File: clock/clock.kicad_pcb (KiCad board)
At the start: 2 copper layers, 176.8 x 81.3 mm, 345 parts, among them P101 CONN_01X03, P102 CONN_FAN_PWM, P103 XG4A-1631, P301 MCRF, P401 CONN_01X10, Q201 MMBT3904, Q301 BSS138, Q302 BSS138, Q401 BSS138, Q402 BSS138, Q501 BSS138, Q502 BSS138, U201 PCA9306, U202 DAC8830, U203 LMV722, U204 LTC2990, U205 LP3853, U207 NC7SZ125, U301 Adafruit746, U302 MIC5225, U303 PA6H, U401 74LVC541, U501 TPS56428, U502 TPS56428, U503 TPS56428, U601 ADT7410, U602 DS3231, U603 ADT7410, Y202 CX210

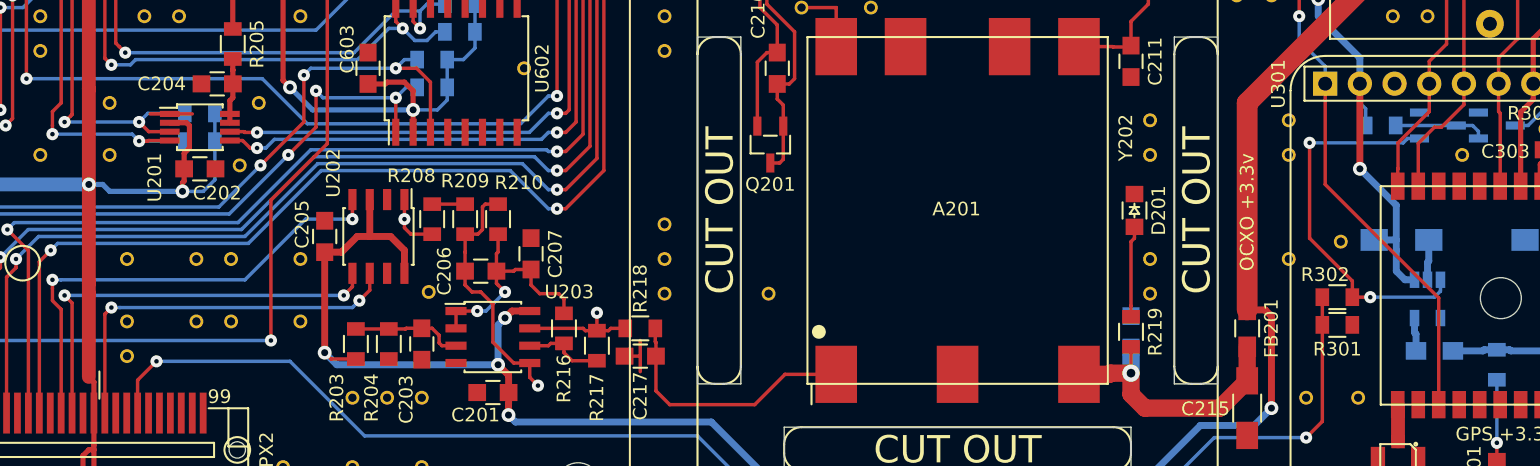
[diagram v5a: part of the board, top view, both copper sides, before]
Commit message: Add DNP to unused resistors on the termination board. Minor clean up of clock board.
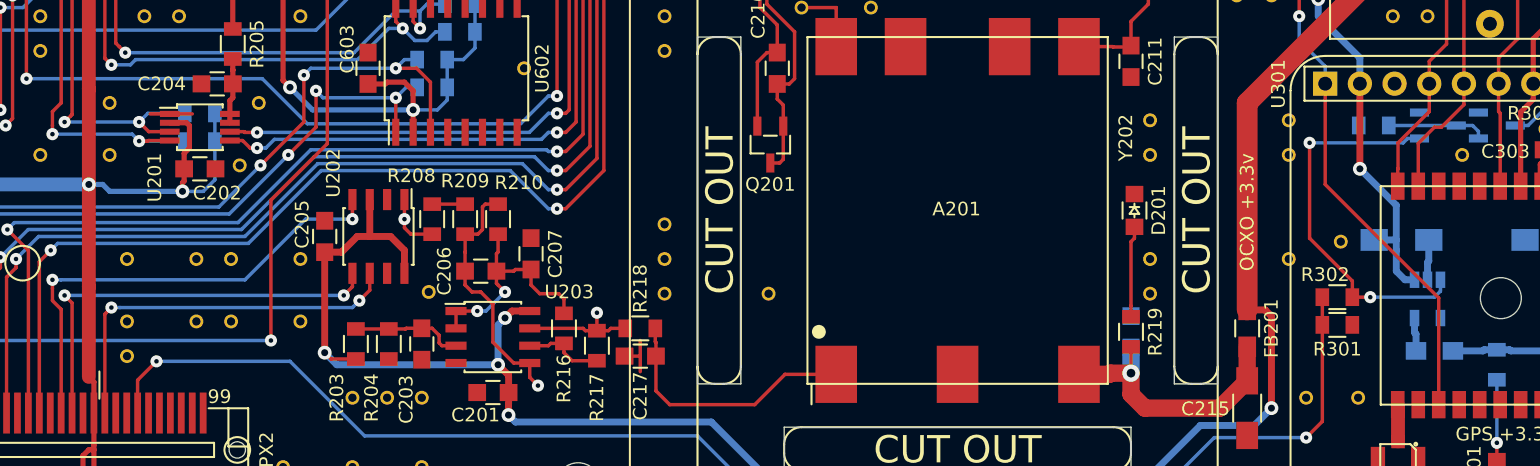
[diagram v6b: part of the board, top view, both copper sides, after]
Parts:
- moved R304 0.51 mm to (346.6, 216.3)
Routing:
- net /gps/~ENA5~: track 6.76 -> 7.27 mm
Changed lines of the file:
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@@
   (general
     (links 646)
-    (no_connects 1)
+    (no_connects 0)
     (area 184.650999 163.286 373.199858 248.171)
     (thickness 1.6)
     (drawings 90)
-    (tracks 1811)
+    (tracks 1809)
     (zones 0)
     (modules 345)
@@
   )
   (module local:R_0805_HandSoldering (layer B.Cu)
-    (at 347.091 216.281 180)
+    (at 346.583 216.281 180)
     (descr "Resistor SMD 0805, hand soldering")
     (tags "resistor 0805")
@@
   (via (at 254 184.404) (size 1.016) (drill 0.6096) (layers F.Cu B.Cu) (net 2))
   (segment (start 233.901 215.646) (end 236.728 215.646) (width 0.381) (layer F.Cu) (net 2) (status 10))
+  (segment (start 252.476 234.696) (end 252.476 228.092) (width 1.016) (layer F.Cu) (net 3))
+  (segment (start 252.476 228.092) (end 252.476 220.598978) (width 1.016) (layer F.Cu) (net 3))
   (segment (start 364.617 197.655) (end 363.771 197.655) (width 0.254) (layer F.Cu) (net 3))
   (segment (start 363.771 197.655) (end 363.601 197.485) (width 0.254) (layer F.Cu) (net 3))
@@
   (via (at 276.225 215.138) (size 1.016) (drill 0.508) (layers F.Cu B.Cu) (net 3))
   (segment (start 361.569 197.485) (end 362.491 197.485) (width 0.381) (layer F.Cu) (net 3) (status 20))
-  (segment (start 252.476 234.696) (end 252.476 228.6) (width 1.016) (layer F.Cu) (net 3))
-  (segment (start 252.476 228.6) (end 252.476 227.838) (width 1.016) (layer F.Cu) (net 3))
-  (segment (start 252.476 227.838) (end 252.476 220.598978) (width 1.016) (layer F.Cu) (net 3))
   (via (at 252.476 220.598978) (size 1.016) (drill 0.508) (layers F.Cu B.Cu) (net 3))
   (segment (start 252.476 213.614008) (end 252.476 220.598978) (width 1.016) (layer F.Cu) (net 3))
   (segment (start 252.476006 213.614002) (end 252.476 213.614008) (width 1.016) (layer F.Cu) (net 3))
+  (segment (start 345.483 216.281) (end 345.483 214.968) (width 0.254) (layer B.Cu) (net 4))
+  (segment (start 345.483 214.968) (end 345.567 214.884) (width 0.254) (layer B.Cu) (net 4))
+  (segment (start 345.567 214.884) (end 345.567 213.217) (width 0.254) (layer B.Cu) (net 4))
   (segment (start 348.234 225.425) (end 348.234 224.663) (width 0.508) (layer B.Cu) (net 4))
   (segment (start 348.234 224.663) (end 348.234 222.123) (width 0.508) (layer B.Cu) (net 4))
@@
   (segment (start 345.567 219.456006) (end 345.567 213.217) (width 0.508) (layer F.Cu) (net 4))
   (segment (start 345.567 211.328) (end 345.567 213.217) (width 0.508) (layer B.Cu) (net 4))
-  (segment (start 345.567 213.217) (end 345.567 214.63) (width 0.254) (layer B.Cu) (net 4))
-  (segment (start 345.991 215.054) (end 345.567 214.63) (width 0.254) (layer B.Cu) (net 4))
-  (segment (start 345.991 216.281) (end 345.991 215.054) (width 0.254) (layer B.Cu) (net 4))
   (via (at 345.567 219.456006) (size 1.016) (drill 0.508) (layers F.Cu B.Cu) (net 4))
   (segment (start 318.008 178.181) (end 319.906 178.181) (width 0.508) (layer B.Cu) (net 5))
@@
   (segment (start 271.145 228.727) (end 271.78 228.092) (width 0.254) (layer F.Cu) (net 49))
   (segment (start 271.78 228.092) (end 271.78 227.109) (width 0.254) (layer F.Cu) (net 49))
-  (segment (start 271.78 229.616) (end 254.755617 229.616) (width 0.254) (layer B.Cu) (net 50))
-  (segment (start 272.288 229.108) (end 271.78 229.616) (width 0.254) (layer B.Cu) (net 50))
-  (segment (start 253.682501 230.060499) (end 254.127 229.616) (width 0.254) (layer F.Cu) (net 50))
   (segment (start 253.6472 237.3427) (end 253.6472 230.0958) (width 0.254) (layer F.Cu) (net 50))
-  (segment (start 253.6472 230.0958) (end 253.682501 230.060499) (width 0.254) (layer F.Cu) (net 50))
+  (segment (start 253.6472 230.0958) (end 253.746 229.997) (width 0.254) (layer F.Cu) (net 50))
+  (segment (start 253.746 229.997) (end 254.127 229.616) (width 0.254) (layer F.Cu) (net 50))
   (segment (start 254.755617 229.616) (end 254.127 229.616) (width 0.254) (layer B.Cu) (net 50))
+  (segment (start 271.78 229.616) (end 254.755617 229.616) (width 0.254) (layer B.Cu) (net 50))
+  (segment (start 272.288 229.108) (end 271.78 229.616) (width 0.254) (layer B.Cu) (net 50))
   (via (at 254.127 229.616) (size 0.889) (drill 0.3302) (layers F.Cu B.Cu) (net 50))
-  (segment (start 254.508 229.616) (end 254.127 229.616) (width 0.254) (layer B.Cu) (net 50))
   (segment (start 273.05 228.346) (end 272.288 229.108) (width 0.254) (layer F.Cu) (net 50))
   (via (at 272.288 229.108) (size 0.889) (drill 0.3302) (layers F.Cu B.Cu) (net 50))
@@
   (segment (start 354.25 216.709) (end 354.25 217.231) (width 0.254) (layer B.Cu) (net 226))
   (segment (start 352.632 216.281) (end 353.822 216.281) (width 0.254) (layer B.Cu) (net 226))
-  (segment (start 348.191 216.281) (end 352.632 216.281) (width 0.254) (layer B.Cu) (net 226))
+  (segment (start 347.683 216.281) (end 352.632 216.281) (width 0.254) (layer B.Cu) (net 226) (status 10))
   (segment (start 356.95 216.281) (end 357.886 216.281) (width 0.254) (layer B.Cu) (net 227))
   (segment (start 357.886 216.281) (end 359.41 214.757) (width 0.254) (layer B.Cu) (net 227))

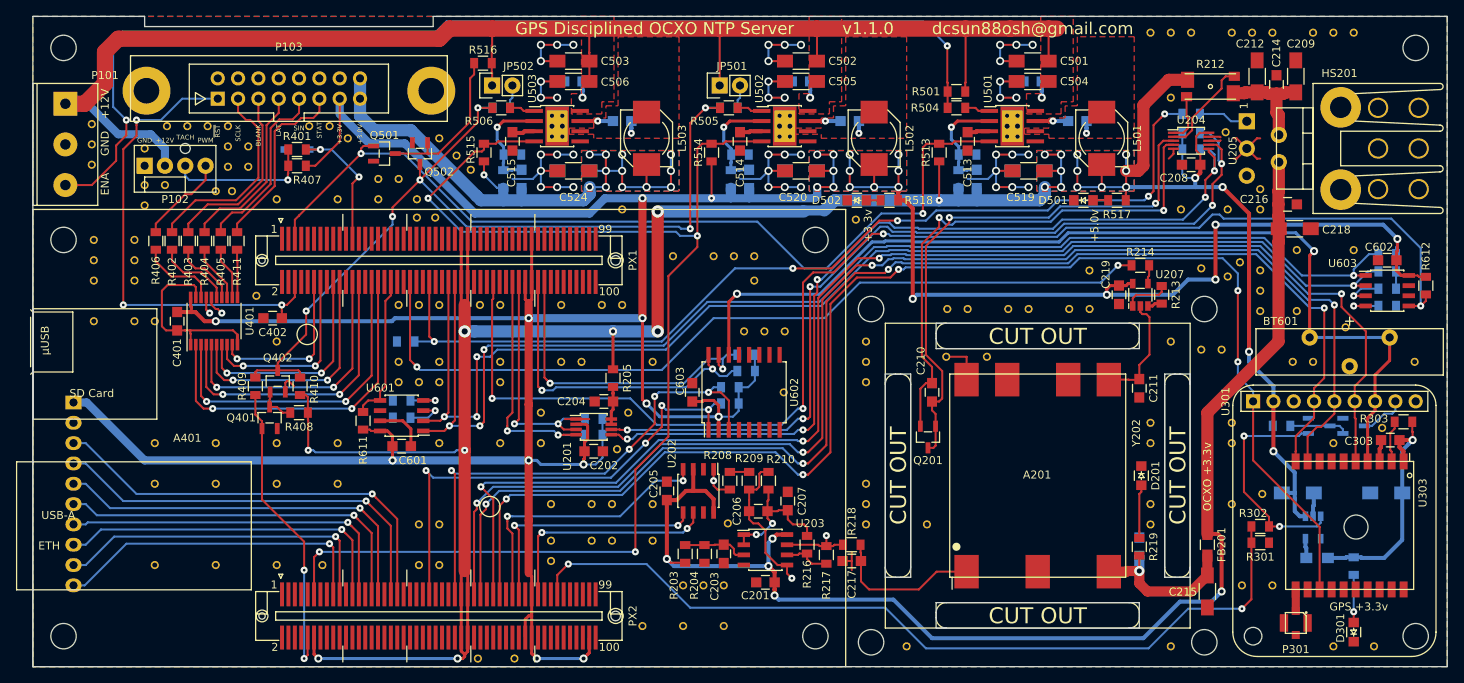
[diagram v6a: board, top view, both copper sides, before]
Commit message: Label more test points.
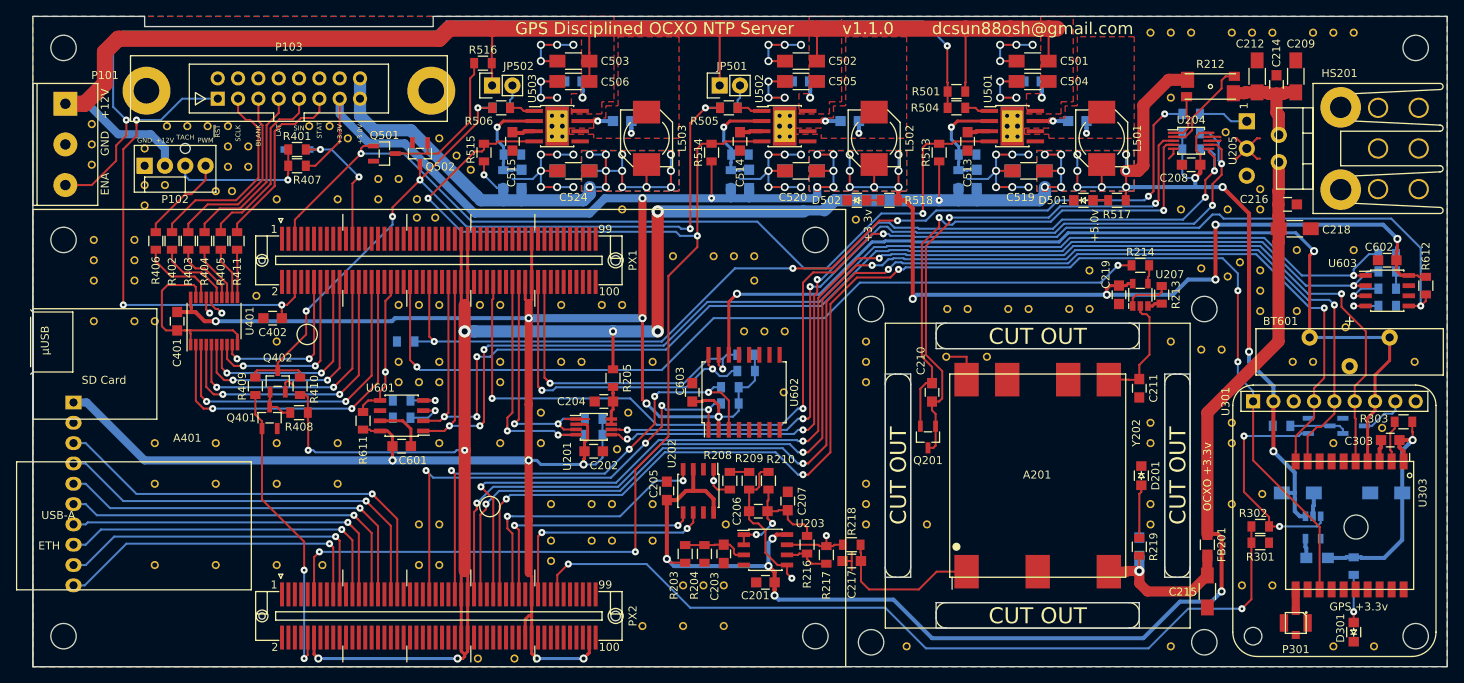
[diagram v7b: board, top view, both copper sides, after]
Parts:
- moved REF** 0.28 mm to (277.1, 228.6)
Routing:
- net /microzed/~INT~1: vias 0 -> 1
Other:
- board text added: "~INT1~"
- board text added: "~INT2~"
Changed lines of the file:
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@@
     (area 184.650999 163.286 373.199858 248.171)
     (thickness 1.6)
-    (drawings 90)
-    (tracks 1809)
+    (drawings 93)
+    (tracks 1812)
     (zones 0)
     (modules 345)
@@
   )
   (module local:Stitching_Via_40x24mil locked (layer F.Cu)
-    (at 277.368 228.473)
+    (at 277.114 228.6)
     (fp_text reference REF** (at 0 1.778) (layer F.SilkS) hide
       (effects (font (size 1 1) (thickness 0.15)))
@@
       (effects (font (size 1 1) (thickness 0.15)))
     )
-    (fp_text user "SD Card" (at 43.434 5.588 180) (layer F.SilkS)
+    (fp_text user "SD Card" (at 41.91 7.239 180) (layer F.SilkS)
       (effects (font (size 1 1) (thickness 0.15)))
     )
@@
     (tags SOT-23)
     (attr smd)
-    (fp_text reference Q502 (at -2.413 -2.286 360) (layer F.SilkS)
+    (fp_text reference Q502 (at -2.54 -1.651 360) (layer F.SilkS)
       (effects (font (size 1 1) (thickness 0.15)))
     )
@@
     )
   )
+  (gr_text ~INT1~ (at 232.029 210.566) (layer B.SilkS)
+    (effects (font (size 0.6 0.6) (thickness 0.127)) (justify mirror))
+  )
+  (gr_line (start 234.569 209.55) (end 233.172 210.439) (layer B.SilkS) (width 0.15))
+  (gr_text ~INT2~ (at 289.814 214.122) (layer B.SilkS)
+    (effects (font (size 0.6 0.6) (thickness 0.127)) (justify mirror))
+  )
   (gr_line (start 286.512 189.23) (end 289.941 189.23) (layer B.Mask) (width 0.508))
   (gr_line (start 273.939 212.09) (end 274.955 212.09) (layer B.SilkS) (width 0.15))
@@
   )
   (gr_line (start 290.576 230.632) (end 289.687 229.997) (layer B.SilkS) (width 0.15))
-  (gr_line (start 238.506 208.915) (end 237.871 209.55) (layer B.SilkS) (width 0.15))
+  (gr_line (start 238.506 208.915) (end 239.268 209.423) (layer B.SilkS) (width 0.15))
   (gr_line (start 249.809 216.916) (end 248.793 217.551) (layer B.SilkS) (width 0.15))
-  (gr_line (start 251.587 214.884) (end 250.698 216.027) (layer B.SilkS) (width 0.15))
+  (gr_line (start 251.206 214.884) (end 250.698 216.027) (layer B.SilkS) (width 0.15))
   (gr_line (start 271.145 228.727) (end 272.796 227.33) (layer B.SilkS) (width 0.15))
   (gr_line (start 272.288 229.108) (end 273.558 229.743) (layer B.SilkS) (width 0.15))
@@
     (effects (font (size 0.6 0.6) (thickness 0.127)) (justify mirror))
   )
-  (gr_text 10MHZ (at 236.22 209.55) (layer B.SilkS)
+  (gr_text 10MHZ (at 240.919 209.423) (layer B.SilkS)
     (effects (font (size 0.6 0.6) (thickness 0.127)) (justify mirror))
   )
@@
     (effects (font (size 0.6 0.6) (thickness 0.127)) (justify mirror))
   )
-  (gr_text OCXO_SCL (at 254 214.884) (layer B.SilkS)
+  (gr_text OCXO_SCL (at 251.079 214.249) (layer B.SilkS)
     (effects (font (size 0.6 0.6) (thickness 0.127)) (justify mirror))
   )
@@
   (via (at 254 184.404) (size 1.016) (drill 0.6096) (layers F.Cu B.Cu) (net 2))
   (segment (start 233.901 215.646) (end 236.728 215.646) (width 0.381) (layer F.Cu) (net 2) (status 10))
+  (segment (start 232.621 216.746) (end 232.791 216.916) (width 0.254) (layer F.Cu) (net 3))
+  (segment (start 232.791 216.916) (end 233.901 216.916) (width 0.254) (layer F.Cu) (net 3))
+  (segment (start 231.775 216.746) (end 232.621 216.746) (width 0.254) (layer F.Cu) (net 3))
   (segment (start 252.476 234.696) (end 252.476 228.092) (width 1.016) (layer F.Cu) (net 3))
   (segment (start 252.476 228.092) (end 252.476 220.598978) (width 1.016) (layer F.Cu) (net 3))
@@
   (segment (start 279.908 211.455) (end 278.722 211.455) (width 0.254) (layer B.Cu) (net 3))
   (segment (start 280.754 207.391) (end 280.754 209.423) (width 0.254) (layer B.Cu) (net 3))
-  (segment (start 231.775 216.746) (end 232.621 216.746) (width 0.254) (layer F.Cu) (net 3))
-  (segment (start 232.621 216.746) (end 232.791 216.916) (width 0.254) (layer F.Cu) (net 3))
-  (segment (start 232.791 216.916) (end 233.901 216.916) (width 0.254) (layer F.Cu) (net 3))
   (segment (start 361.061 192.913) (end 361.061 193.802) (width 0.254) (layer B.Cu) (net 3))
   (segment (start 360.891 193.972) (end 360.891 194.818) (width 0.254) (layer B.Cu) (net 3))
@@
   (segment (start 252.476 213.614008) (end 252.476 220.598978) (width 1.016) (layer F.Cu) (net 3))
   (segment (start 252.476006 213.614002) (end 252.476 213.614008) (width 1.016) (layer F.Cu) (net 3))
+  (segment (start 303.784 183.218) (end 303.784 188.087) (width 0.254) (layer F.Cu) (net 4))
   (segment (start 345.483 216.281) (end 345.483 214.968) (width 0.254) (layer B.Cu) (net 4))
   (segment (start 345.483 214.968) (end 345.567 214.884) (width 0.254) (layer B.Cu) (net 4))
@@
   (segment (start 306.197 186.52) (end 306.197 188.087) (width 1.27) (layer B.Cu) (net 4))
   (via (at 303.784 188.087) (size 0.889) (drill 0.3302) (layers F.Cu B.Cu) (net 4))
-  (segment (start 303.784 188.087) (end 303.784 183.468) (width 0.254) (layer F.Cu) (net 4))
   (segment (start 316.357 188.087) (end 316.992 187.452) (width 1.524) (layer B.Cu) (net 4))
   (segment (start 316.992 187.452) (end 316.992 186.436) (width 1.524) (layer B.Cu) (net 4))
@@
   (segment (start 323.018 188.087) (end 324.909 188.087) (width 0.254) (layer F.Cu) (net 237))
   (segment (start 294.697 188.087) (end 296.461 188.087) (width 0.254) (layer F.Cu) (net 238))
+  (segment (start 231.775 213.741) (end 232.41 213.106) (width 0.254) (layer F.Cu) (net 239))
+  (segment (start 232.41 213.106) (end 232.791 213.106) (width 0.254) (layer F.Cu) (net 239))
+  (segment (start 231.775 214.546) (end 231.775 213.741) (width 0.254) (layer F.Cu) (net 239))
+  (segment (start 234.569 209.55) (end 234.569 211.328) (width 0.254) (layer F.Cu) (net 239))
+  (segment (start 234.569 211.328) (end 233.901 211.996) (width 0.254) (layer F.Cu) (net 239))
   (segment (start 235.2472 198.2927) (end 235.2472 199.9818) (width 0.254) (layer F.Cu) (net 239))
   (segment (start 235.2472 199.9818) (end 234.569 200.66) (width 0.254) (layer F.Cu) (net 239))
-  (segment (start 234.569 200.66) (end 234.569 211.328) (width 0.254) (layer F.Cu) (net 239))
-  (segment (start 234.569 211.328) (end 233.901 211.996) (width 0.254) (layer F.Cu) (net 239))
+  (segment (start 234.569 200.66) (end 234.569 209.55) (width 0.254) (layer F.Cu) (net 239))
+  (via (at 234.569 209.55) (size 0.889) (drill 0.3302) (layers F.Cu B.Cu) (net 239))
+  (segment (start 232.791 213.106) (end 233.901 213.106) (width 0.254) (layer F.Cu) (net 239))
   (segment (start 233.901 211.996) (end 233.901 213.106) (width 0.254) (layer F.Cu) (net 239))
-  (segment (start 232.41 213.106) (end 231.775 213.741) (width 0.254) (layer F.Cu) (net 239))
-  (segment (start 231.775 213.741) (end 231.775 214.546) (width 0.254) (layer F.Cu) (net 239))
-  (segment (start 233.901 213.106) (end 232.41 213.106) (width 0.254) (layer F.Cu) (net 239))
   (segment (start 296.799 192.278) (end 297.434 192.278) (width 0.254) (layer B.Cu) (net 240))
   (segment (start 318.516 192.659) (end 319.659 191.516) (width 0.254) (layer B.Cu) (net 240))

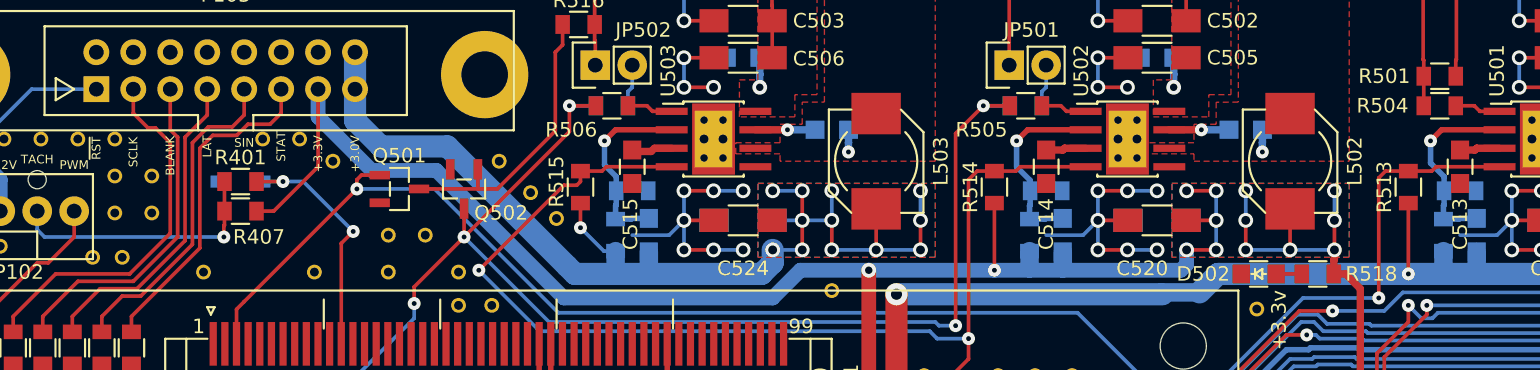
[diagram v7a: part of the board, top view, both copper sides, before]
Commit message: Change placement of fan tachometer input components.
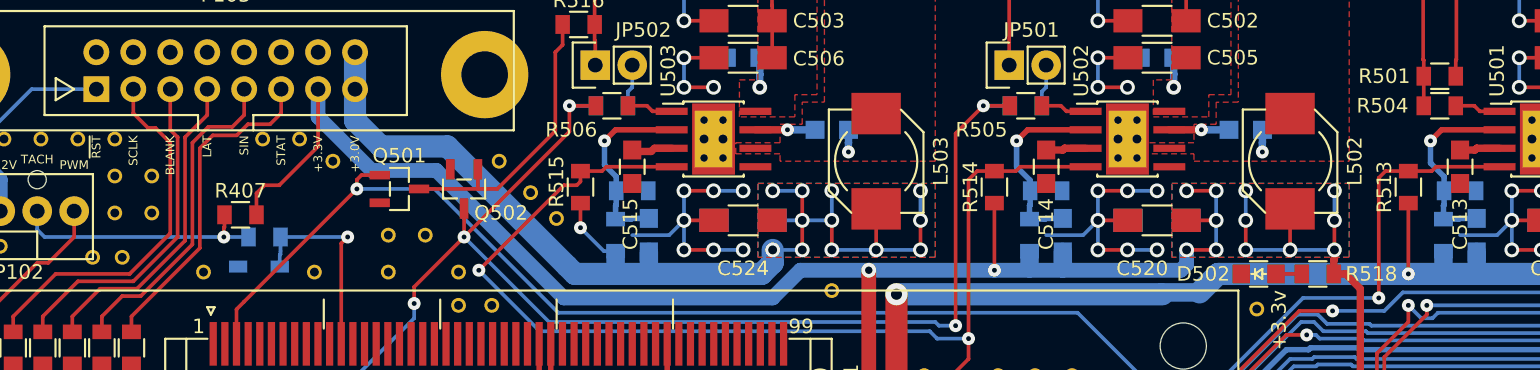
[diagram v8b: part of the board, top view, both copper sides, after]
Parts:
- R401: moved to B.Cu
- moved D401 5.98 mm to (224.8, 187.6)
- moved R401 4.15 mm to (225.2, 185.5)
- moved R407 0.25 mm to (223.5, 184.0)
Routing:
- net /microzed/TACH: track 17.6 -> 14.2 mm, vias 2 -> 1
- net /microzed/FAN_TACH: track 18.1 -> 17.5 mm
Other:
- net class Default: clearance 0.254 -> 0.253746
- rule trace_clearance: 0.254 -> 0.253746
